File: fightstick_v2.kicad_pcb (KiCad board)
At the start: 2 copper layers, 233 x 125.9 mm, 159 parts, among them J1 USB_C_Receptacle_USB2.0, J2 Conn_01x04, J3 Conn_01x03, J9 Conn_01x05, SW1 SW_Push, SW10 SW_Push, SW11 SW_Push, SW12 SW_Push, SW13 SW_Push, SW14 SW_Push, SW15 SW_Push, SW16 SW_Push, SW17 SW_Push, SW19 SW_Push, SW2 SW_Push, SW3 SW_Push, SW4 SW_Push, SW5 SW_Push, SW6 SW_Push, SW7 SW_Push, SW8 SW_Push, SW9 SW_Push, U1 XC6206PxxxMR, U2 W25Q128JVS, U3 RP2040, U4 SRV05-4, U5 74AHCT1G125, Y1 12MHz

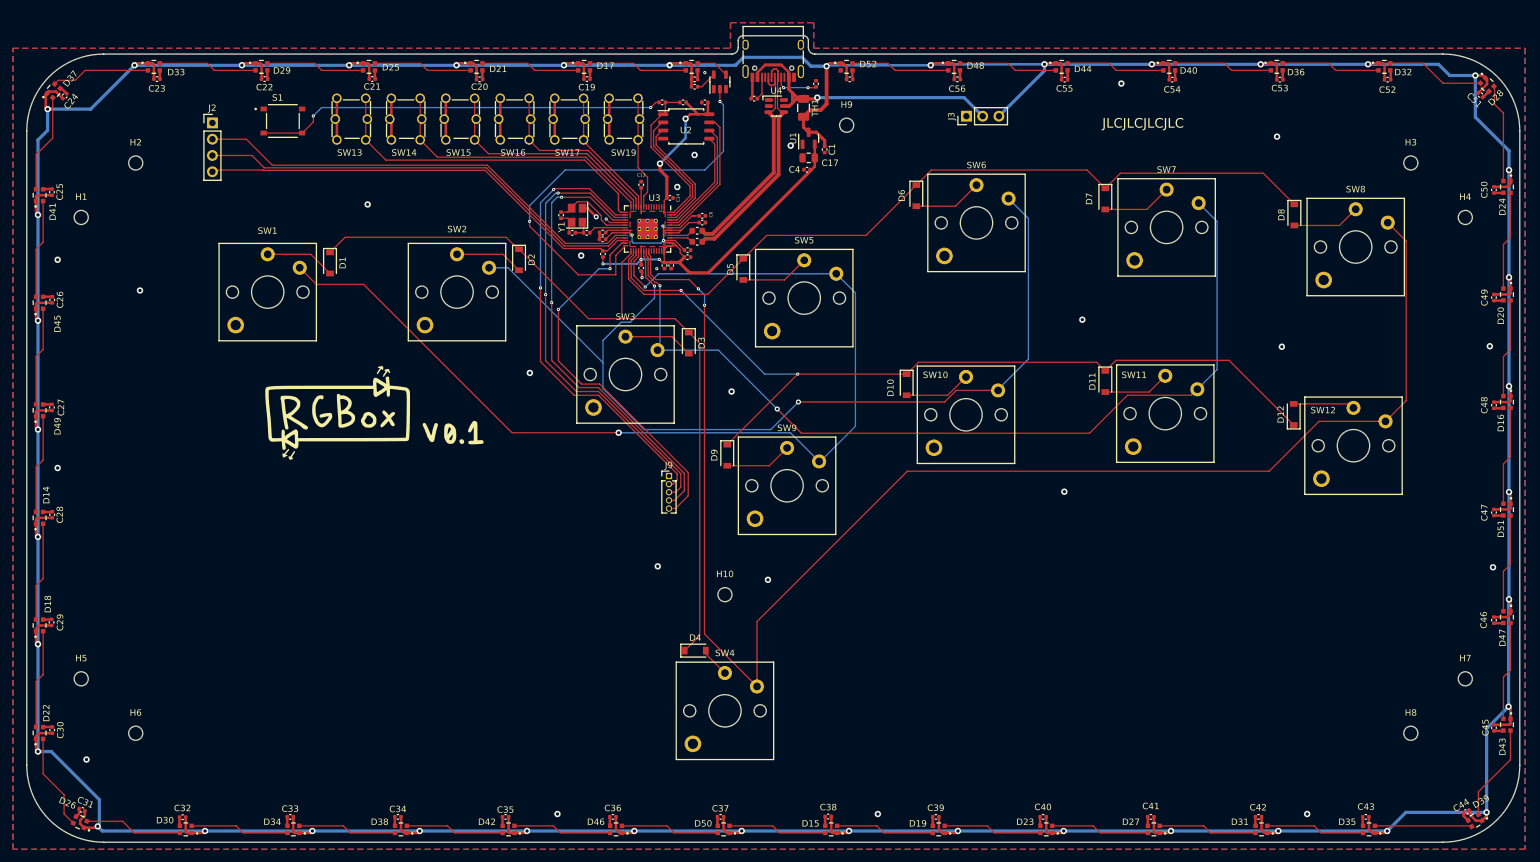
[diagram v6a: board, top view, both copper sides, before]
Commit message: last update for now on sk6812 ver
these are the files im submitting to jlc. im thinking about making a version with dumb led's which would save me about $10 minimum but that will go on a different branch
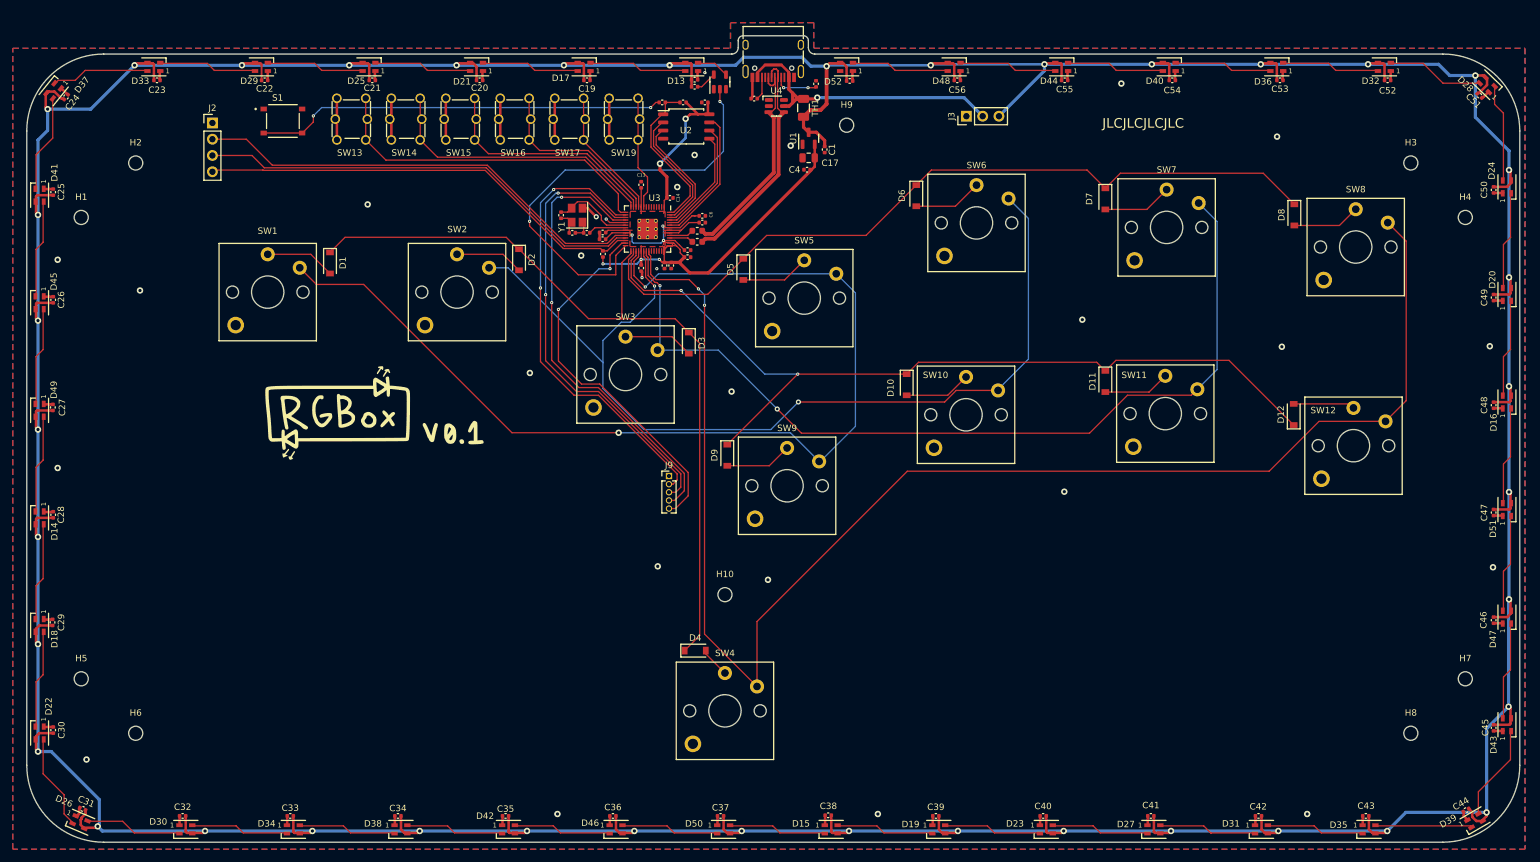
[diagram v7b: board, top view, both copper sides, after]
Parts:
- D13, D14, D15, D16, D17, D18, D19, D20, D21, D22, D23, D24, D25, D26, D27, D28, D29, D30, D31, D32, D33, D34, D35, D36, D37, D38, D39, D40, D41, D42, D43, D44, D45, D46, D47, D48, D49, D50, D51, D52: value WS2812C-2020 -> SK6812; footprint components:LED_WS2812-2020 -> LED_SMD:LED_SK6805_PLCC4_2.4x2.7mm_P1.3mm
- moved C44 0.25 mm to (270.8, 141.9)
- moved C57 0.25 mm to (174.6, 28.1)
- moved C24 0.25 mm to (52.3, 30.6)
- moved C38 0.20 mm to (171.2, 142.7)
- moved C19 0.20 mm to (133.6, 28.0)
- moved C21 0.20 mm to (100.1, 28.0)
- moved C22 0.20 mm to (83.3, 28.0)
- moved C23 0.20 mm to (66.5, 28.0)
- moved C25 0.20 mm to (50.3, 45.5)
- moved C32 0.20 mm to (70.5, 142.8)
- moved C51 0.18 mm to (272.9, 30.4)
- moved C31 0.18 mm to (54.9, 141.7)
- moved C29 0.15 mm to (50.2, 112.6)
- moved C20 0.15 mm to (116.8, 28.0)
- moved C26 0.15 mm to (50.3, 62.2)
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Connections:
- D13 pad 1: +5V -> GND
- D13 pad 2: Net-(D13-Pad2) -> D_ARGB_5V
- D13 pad 3: GND -> +5V
- D13 pad 4: D_ARGB_5V -> Net-(D13-Pad4)
- D14 pad 1: +5V -> GND
- D14 pad 3: GND -> +5V
- D15 pad 1: +5V -> GND
- D15 pad 3: GND -> +5V
- D16 pad 1: +5V -> GND
- D16 pad 3: GND -> +5V
- D17 pad 1: +5V -> GND
- D17 pad 2: Net-(D17-Pad2) -> Net-(D13-Pad4)
- D17 pad 3: GND -> +5V
- D17 pad 4: Net-(D13-Pad2) -> Net-(D17-Pad4)
- D18 pad 1: +5V -> GND
- D18 pad 2: Net-(D18-Pad2) -> Net-(D14-Pad4)
- D18 pad 3: GND -> +5V
- D18 pad 4: Net-(D14-Pad2) -> Net-(D18-Pad4)
- D19 pad 1: +5V -> GND
- D19 pad 2: Net-(D19-Pad2) -> Net-(D15-Pad4)
- D19 pad 3: GND -> +5V
- D19 pad 4: Net-(D15-Pad2) -> Net-(D19-Pad4)
- D20 pad 1: +5V -> GND
- D20 pad 2: Net-(D20-Pad2) -> Net-(D16-Pad4)
- D20 pad 3: GND -> +5V
- D20 pad 4: Net-(D16-Pad2) -> Net-(D20-Pad4)
- D21 pad 1: +5V -> GND
- D21 pad 2: Net-(D21-Pad2) -> Net-(D17-Pad4)
- D21 pad 3: GND -> +5V
- D21 pad 4: Net-(D17-Pad2) -> Net-(D21-Pad4)
- D22 pad 1: +5V -> GND
- D22 pad 2: Net-(D22-Pad2) -> Net-(D18-Pad4)
- D22 pad 3: GND -> +5V
- D22 pad 4: Net-(D18-Pad2) -> Net-(D22-Pad4)
- D23 pad 1: +5V -> GND
- D23 pad 2: Net-(D23-Pad2) -> Net-(D19-Pad4)
- D23 pad 3: GND -> +5V
- D23 pad 4: Net-(D19-Pad2) -> Net-(D23-Pad4)
- D24 pad 1: +5V -> GND
- D24 pad 2: Net-(D24-Pad2) -> Net-(D20-Pad4)
- D24 pad 3: GND -> +5V
- D24 pad 4: Net-(D20-Pad2) -> Net-(D24-Pad4)
- D25 pad 1: +5V -> GND
- D25 pad 2: Net-(D25-Pad2) -> Net-(D21-Pad4)
- D25 pad 3: GND -> +5V
- D25 pad 4: Net-(D21-Pad2) -> Net-(D25-Pad4)
- D26 pad 1: +5V -> GND
- D26 pad 2: Net-(D26-Pad2) -> Net-(D22-Pad4)
- D26 pad 3: GND -> +5V
- D26 pad 4: Net-(D22-Pad2) -> Net-(D26-Pad4)
- D27 pad 1: +5V -> GND
- D27 pad 2: Net-(D27-Pad2) -> Net-(D23-Pad4)
- D27 pad 3: GND -> +5V
- D27 pad 4: Net-(D23-Pad2) -> Net-(D27-Pad4)
- D28 pad 1: +5V -> GND
- D28 pad 2: Net-(D28-Pad2) -> Net-(D24-Pad4)
- D28 pad 3: GND -> +5V
- D28 pad 4: Net-(D24-Pad2) -> Net-(D28-Pad4)
- D29 pad 1: +5V -> GND
- D29 pad 2: Net-(D29-Pad2) -> Net-(D25-Pad4)
- D29 pad 3: GND -> +5V
- D29 pad 4: Net-(D25-Pad2) -> Net-(D29-Pad4)
- D30 pad 1: +5V -> GND
- D30 pad 2: Net-(D30-Pad2) -> Net-(D26-Pad4)
- D30 pad 3: GND -> +5V
- D30 pad 4: Net-(D26-Pad2) -> Net-(D30-Pad4)
- D31 pad 1: +5V -> GND
- D31 pad 2: Net-(D31-Pad2) -> Net-(D27-Pad4)
- D31 pad 3: GND -> +5V
- D31 pad 4: Net-(D27-Pad2) -> Net-(D31-Pad4)
- D32 pad 1: +5V -> GND
- D32 pad 2: Net-(D32-Pad2) -> Net-(D28-Pad4)
- D32 pad 3: GND -> +5V
- D32 pad 4: Net-(D28-Pad2) -> Net-(D32-Pad4)
- D33 pad 1: +5V -> GND
- D33 pad 2: Net-(D33-Pad2) -> Net-(D29-Pad4)
- D33 pad 3: GND -> +5V
- D33 pad 4: Net-(D29-Pad2) -> Net-(D33-Pad4)
- D34 pad 1: +5V -> GND
- D34 pad 2: Net-(D34-Pad2) -> Net-(D30-Pad4)
- D34 pad 3: GND -> +5V
- D34 pad 4: Net-(D30-Pad2) -> Net-(D34-Pad4)
- D35 pad 1: +5V -> GND
- D35 pad 2: Net-(D35-Pad2) -> Net-(D31-Pad4)
- D35 pad 3: GND -> +5V
- D35 pad 4: Net-(D31-Pad2) -> Net-(D35-Pad4)
- D36 pad 1: +5V -> GND
- D36 pad 2: Net-(D36-Pad2) -> Net-(D32-Pad4)
- D36 pad 3: GND -> +5V
- D36 pad 4: Net-(D32-Pad2) -> Net-(D36-Pad4)
- D37 pad 1: +5V -> GND
- D37 pad 2: Net-(D37-Pad2) -> Net-(D33-Pad4)
- D37 pad 3: GND -> +5V
- D37 pad 4: Net-(D33-Pad2) -> Net-(D37-Pad4)
- D38 pad 1: +5V -> GND
- D38 pad 2: Net-(D38-Pad2) -> Net-(D34-Pad4)
- D38 pad 3: GND -> +5V
- D38 pad 4: Net-(D34-Pad2) -> Net-(D38-Pad4)
- D39 pad 1: +5V -> GND
- D39 pad 2: Net-(D39-Pad2) -> Net-(D35-Pad4)
- D39 pad 3: GND -> +5V
- D39 pad 4: Net-(D35-Pad2) -> Net-(D39-Pad4)
- D40 pad 1: +5V -> GND
- D40 pad 2: Net-(D40-Pad2) -> Net-(D36-Pad4)
- D40 pad 3: GND -> +5V
- D40 pad 4: Net-(D36-Pad2) -> Net-(D40-Pad4)
- D41 pad 1: +5V -> GND
- D41 pad 2: Net-(D41-Pad2) -> Net-(D37-Pad4)
- D41 pad 3: GND -> +5V
- D41 pad 4: Net-(D37-Pad2) -> Net-(D41-Pad4)
- D42 pad 1: +5V -> GND
- D42 pad 2: Net-(D42-Pad2) -> Net-(D38-Pad4)
- D42 pad 3: GND -> +5V
- D42 pad 4: Net-(D38-Pad2) -> Net-(D42-Pad4)
- D43 pad 1: +5V -> GND
- D43 pad 2: Net-(D43-Pad2) -> Net-(D39-Pad4)
- D43 pad 3: GND -> +5V
- D43 pad 4: Net-(D39-Pad2) -> Net-(D43-Pad4)
- D44 pad 1: +5V -> GND
- D44 pad 2: Net-(D44-Pad2) -> Net-(D40-Pad4)
- D44 pad 3: GND -> +5V
- D44 pad 4: Net-(D40-Pad2) -> Net-(D44-Pad4)
- D45 pad 1: +5V -> GND
- D45 pad 2: Net-(D45-Pad2) -> Net-(D41-Pad4)
- D45 pad 3: GND -> +5V
- D45 pad 4: Net-(D41-Pad2) -> Net-(D45-Pad4)
- D46 pad 1: +5V -> GND
- D46 pad 2: Net-(D46-Pad2) -> Net-(D42-Pad4)
- D46 pad 3: GND -> +5V
- D46 pad 4: Net-(D42-Pad2) -> Net-(D46-Pad4)
- D47 pad 1: +5V -> GND
- D47 pad 2: Net-(D47-Pad2) -> Net-(D43-Pad4)
- D47 pad 3: GND -> +5V
- D47 pad 4: Net-(D43-Pad2) -> Net-(D47-Pad4)
- D48 pad 1: +5V -> GND
- D48 pad 2: Net-(D48-Pad2) -> Net-(D44-Pad4)
- D48 pad 3: GND -> +5V
- D48 pad 4: Net-(D44-Pad2) -> Net-(D48-Pad4)
- D49 pad 1: +5V -> GND
- D49 pad 2: Net-(D14-Pad4) -> Net-(D45-Pad4)
- D49 pad 3: GND -> +5V
- D49 pad 4: Net-(D45-Pad2) -> Net-(D14-Pad2)
- D50 pad 1: +5V -> GND
- D50 pad 2: Net-(D15-Pad4) -> Net-(D46-Pad4)
- D50 pad 3: GND -> +5V
- D50 pad 4: Net-(D46-Pad2) -> Net-(D15-Pad2)
- D51 pad 1: +5V -> GND
- D51 pad 2: Net-(D16-Pad4) -> Net-(D47-Pad4)
- D51 pad 3: GND -> +5V
- D51 pad 4: Net-(D47-Pad2) -> Net-(D16-Pad2)
- D52 pad 1: +5V -> GND
- D52 pad 2: unconnected-(D52-Pad2) -> Net-(D48-Pad4)
- D52 pad 3: GND -> +5V
- D52 pad 4: Net-(D48-Pad2) -> unconnected-(D52-Pad4)
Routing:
- net Net-(D33-Pad4): track 0.00 -> 15.5 mm
- net Net-(D33-Pad2): track 15.5 -> 0.00 mm
- net Net-(D27-Pad4): track 0.00 -> 15.5 mm
- net Net-(D27-Pad2): track 15.5 -> 0.00 mm
- net Net-(D20-Pad4): track 0.00 -> 15.4 mm
- net Net-(D20-Pad2): track 15.4 -> 0.00 mm
- net Net-(D44-Pad4): track 0.00 -> 15.4 mm
- net Net-(D44-Pad2): track 15.4 -> 0.00 mm
- net Net-(D36-Pad4): track 0.00 -> 15.4 mm
- net Net-(D36-Pad2): track 15.4 -> 0.00 mm
- net Net-(D13-Pad4): track 0.00 -> 15.4 mm
- net Net-(D13-Pad2): track 15.4 -> 0.00 mm
- net Net-(D46-Pad4): track 0.00 -> 15.4 mm
- net Net-(D46-Pad2): track 15.4 -> 0.00 mm
- net Net-(D41-Pad4): track 0.00 -> 15.4 mm
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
